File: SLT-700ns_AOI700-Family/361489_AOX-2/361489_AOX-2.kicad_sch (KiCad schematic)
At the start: 10 parts, among them U1 12-Pin_SLx_Can

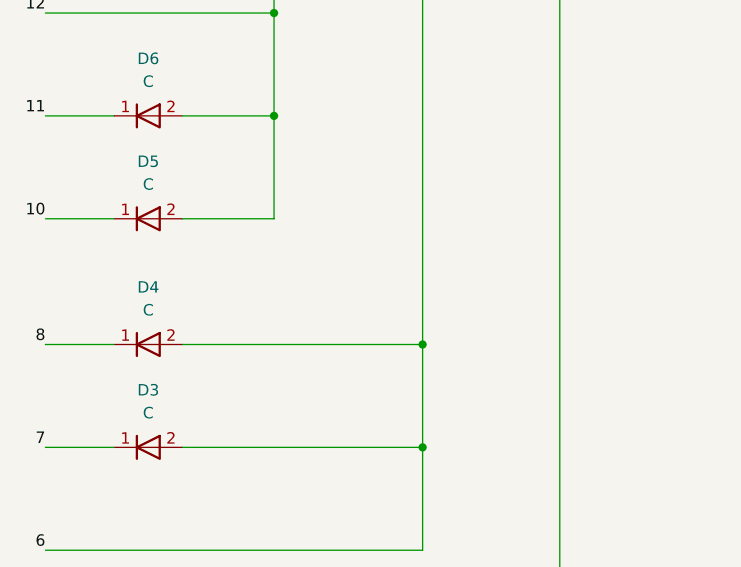
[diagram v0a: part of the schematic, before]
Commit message: Add can P/N to schematics for SLT-700
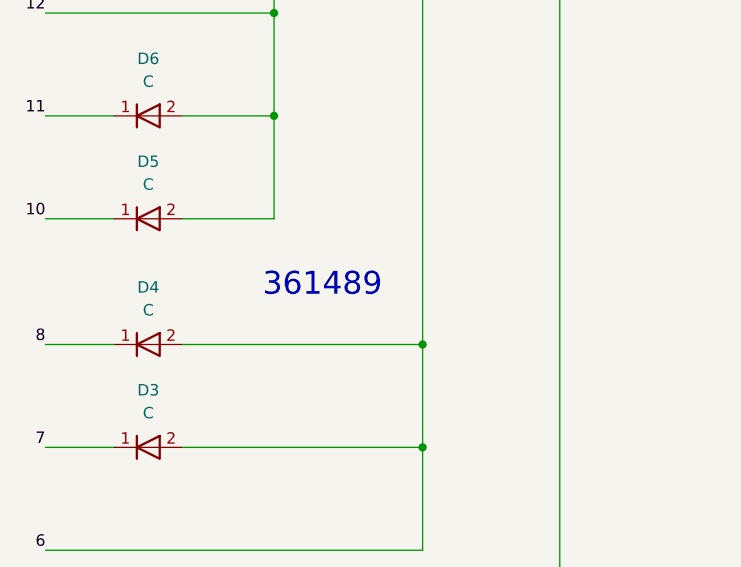
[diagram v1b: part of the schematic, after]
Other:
- note added: "361489"
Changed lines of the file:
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@@
     (effects (font (size 1.27 1.27)) (justify left bottom))
+  )
+  (text "361489" (at 97.79 99.06 0)
+    (effects (font (size 2.54 2.54)) (justify left bottom))
   )
   (label "8" (at 73.66 104.14 180)
